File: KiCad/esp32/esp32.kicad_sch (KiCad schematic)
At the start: 2 parts, among them U1 ESD7104MUTAG, U2 ESP32-S3-MINI-1-N8

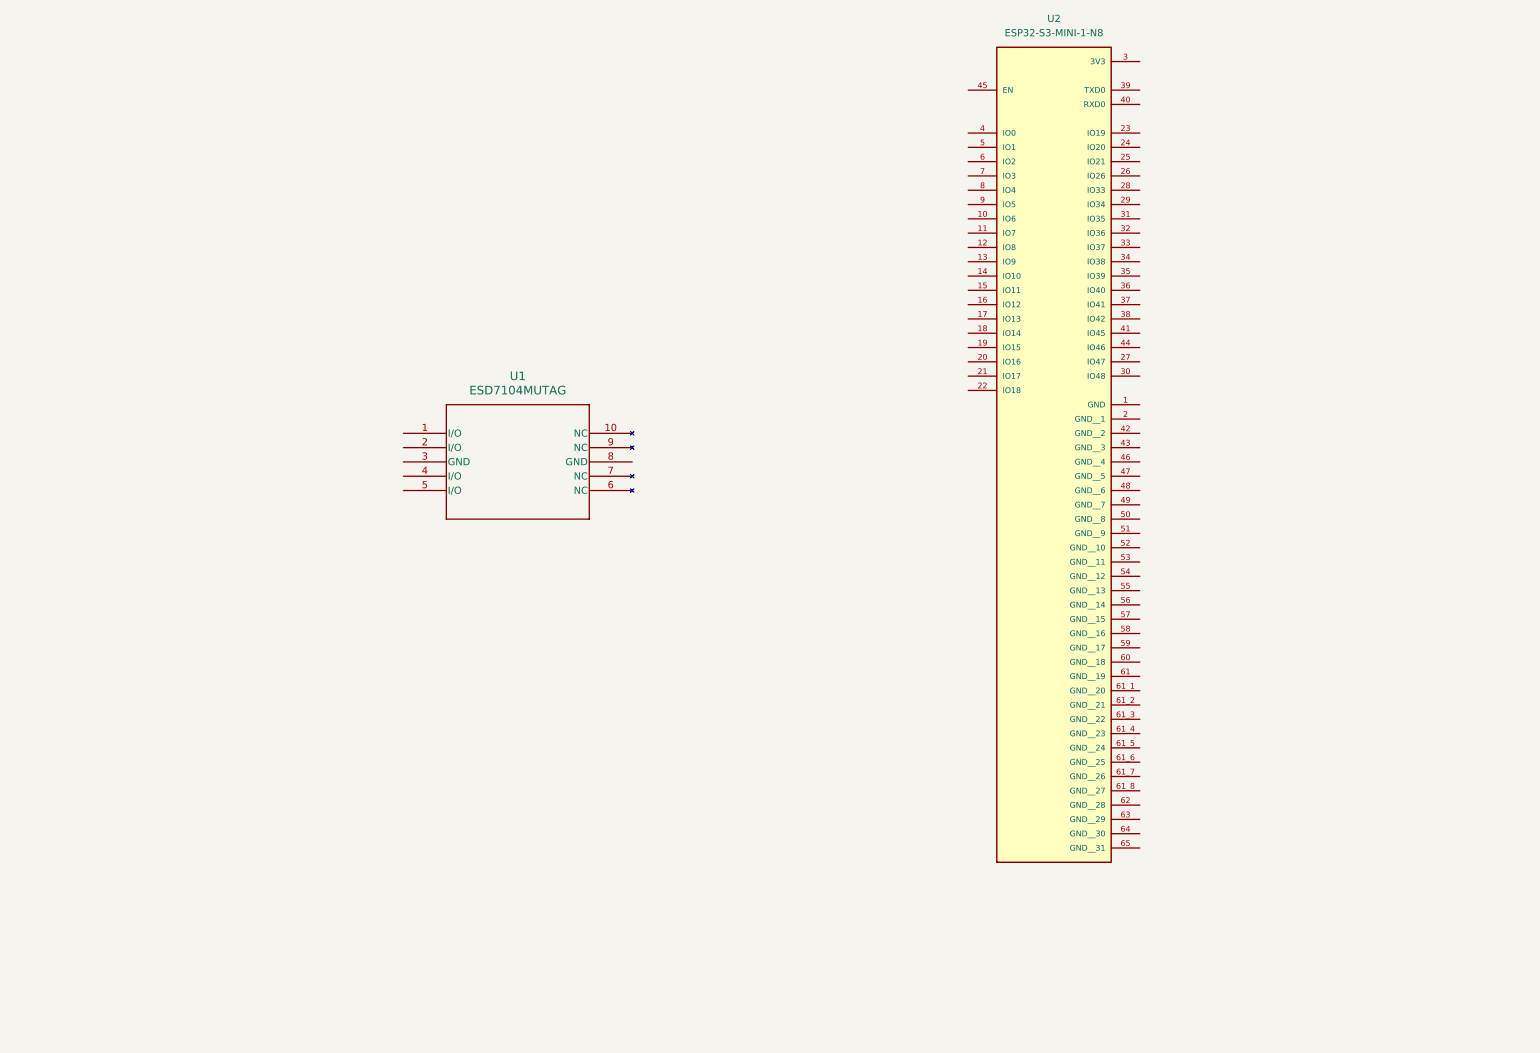
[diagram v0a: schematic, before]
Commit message: restructed the path and file strcter
upaded schiemate and update pcb layout
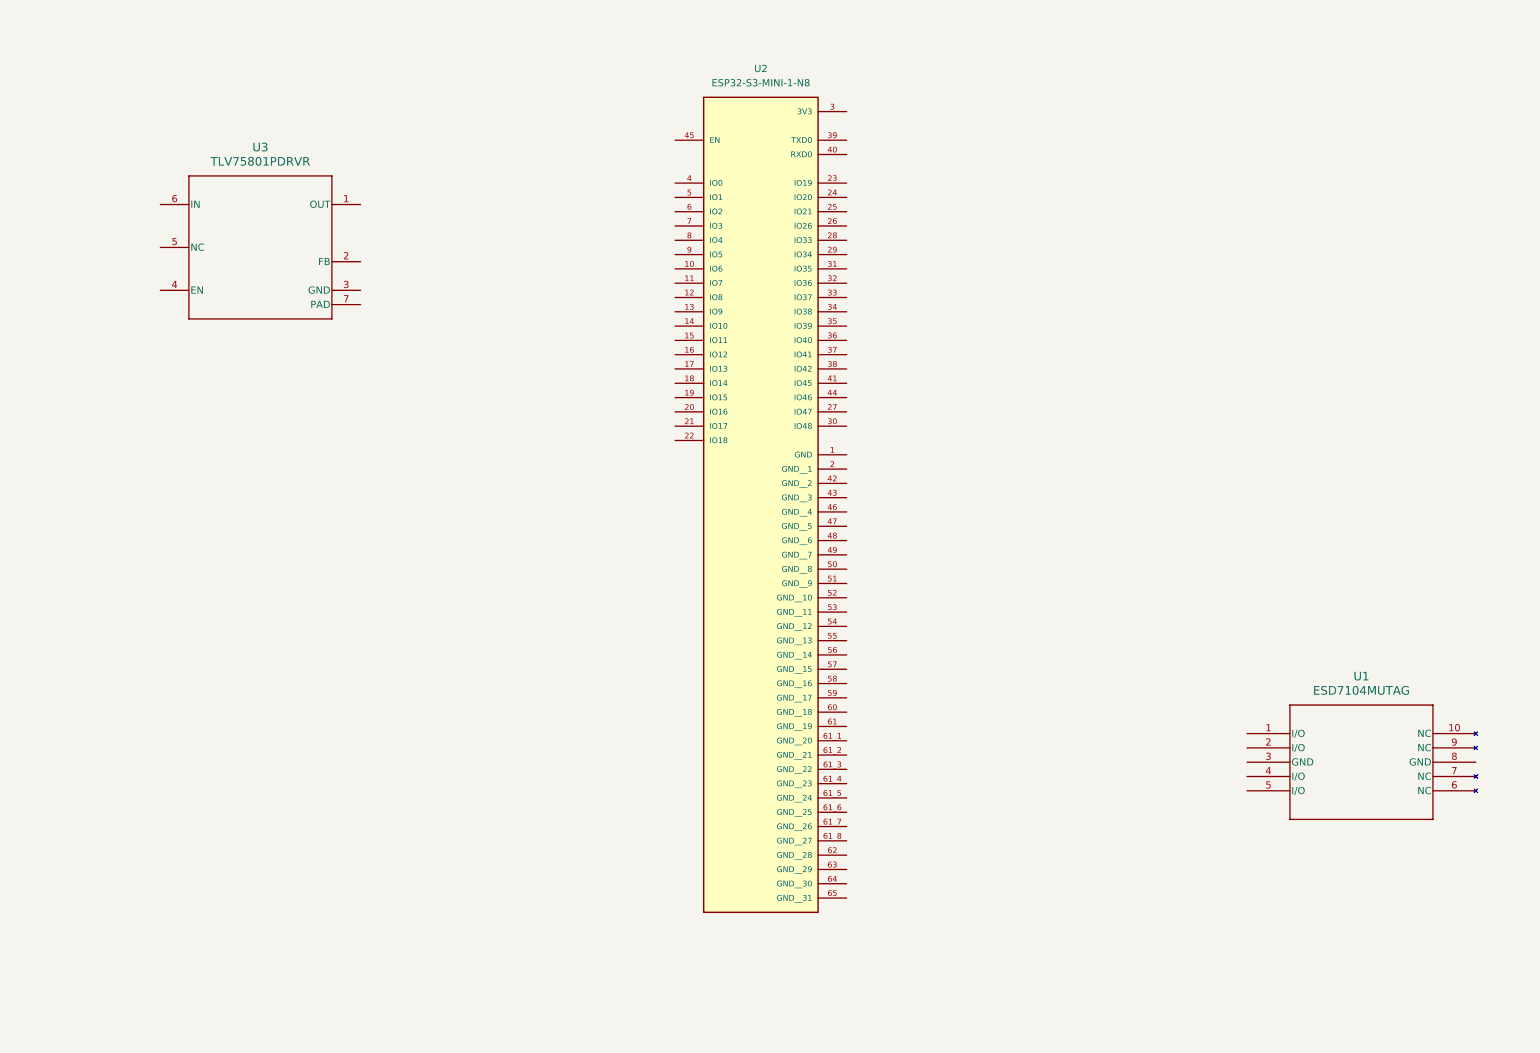
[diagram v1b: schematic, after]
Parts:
- removed U1: ESD7104MUTAG, footprints:UDFN10_ONS-L, symbol 2025-12-02_02-43-39:ESD7104MUTAG
- added U1: ESD7104MUTAG, Footprint:UDFN10_ONS, symbol ESD7104MUTAG:ESD7104MUTAG
- added U3: TLV75801PDRVR, Footprint:DRV0006A, symbol TLV75801PDRVR:TLV75801PDRVR
- U2: footprint ESP32_S3_MINI_1_N8:XCVR_ESP32-S3-MINI-1-N8 -> Footprint:XCVR_ESP32-S3-MINI-1-N8

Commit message: Added all symbols
dowloaded and added all symbols expect for boot/restart
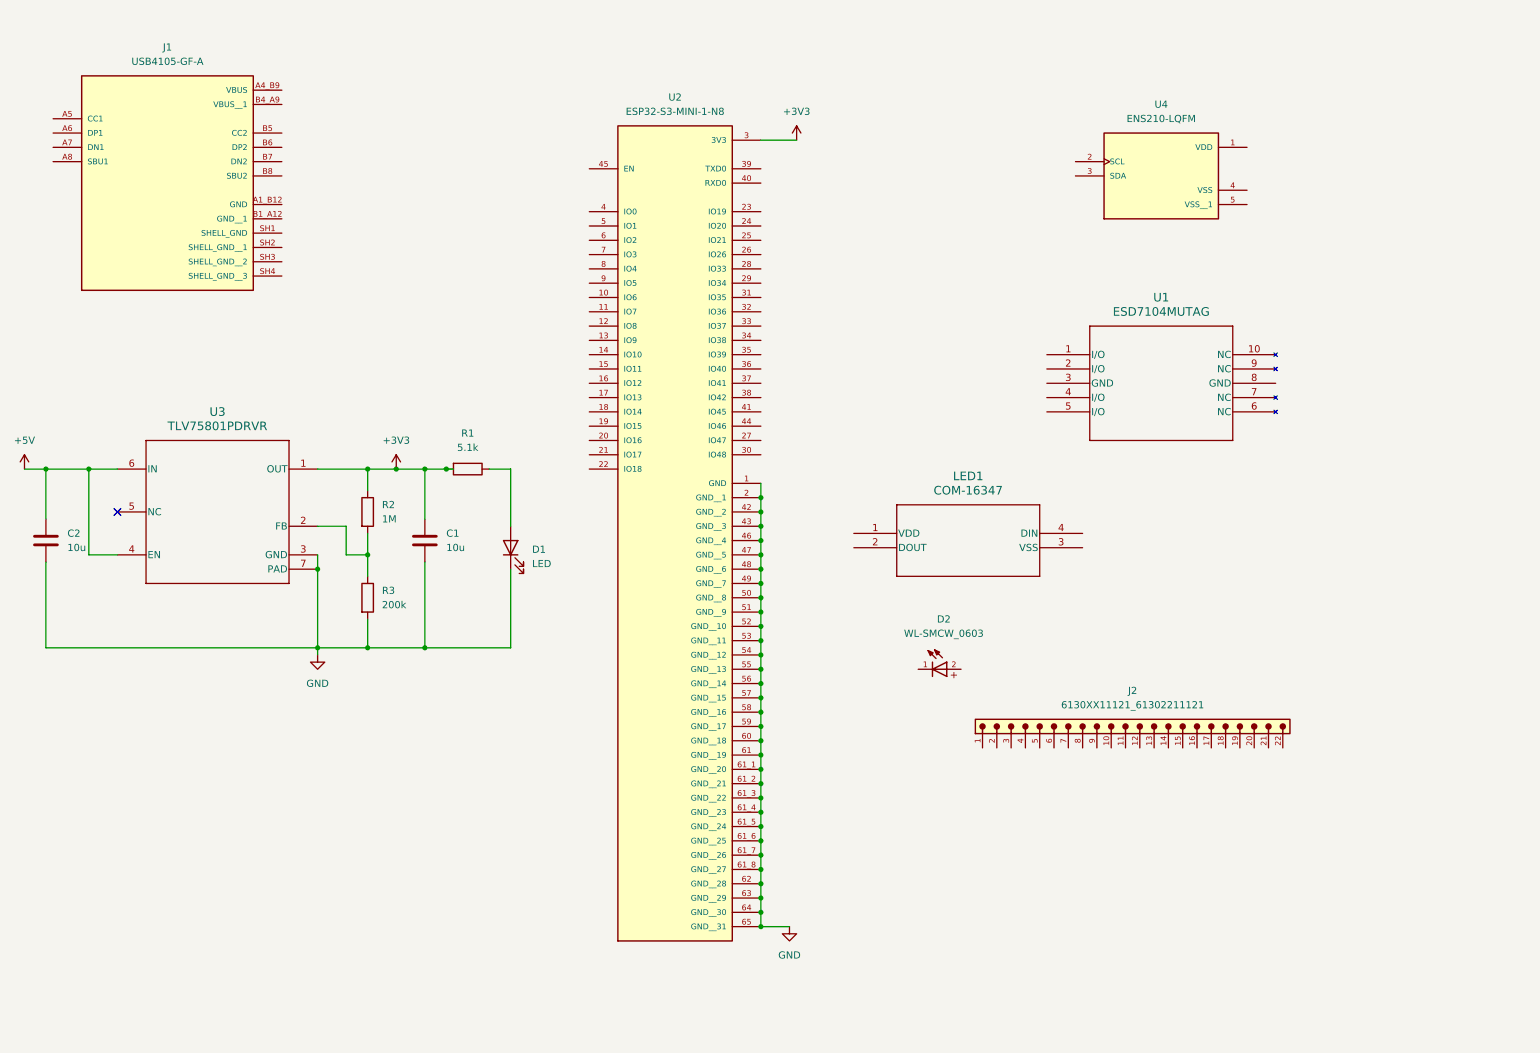
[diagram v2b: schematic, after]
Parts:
- added C1, C2: 10u, Capacitor_SMD:C_0603_1608Metric, symbol Device:C
- added D1: LED, LED_SMD:LED_0603_1608Metric, symbol Device:LED
- added D2: WL-SMCW_0603, WL-SMCW_0603:WL-SMCW_0603, symbol WL-SMCW_0603:WL-SMCW_0603
- added J1: USB4105-GF-A, USB4105-GF-A:GCT_USB4105-GF-A, symbol USB4105-GF-A:USB4105-GF-A
- added J2: 6130XX11121_61302211121, 6130XX11121_61302211121:61302211121, symbol 6130XX11121_61302211121:6130XX11121_61302211121
- added LED1: COM-16347, Footprint:COM-16347_SPK, symbol COM-16347:COM-16347
- added R1: 5.1k, Resistor_SMD:R_0603_1608Metric, symbol Device:R
- added R2: 1M, Resistor_SMD:R_0603_1608Metric, symbol Device:R
- added R3: 200k, Resistor_SMD:R_0603_1608Metric, symbol Device:R
- added U4: ENS210-LQFM, ENS210-LQFM:XDCR_ENS210-LQFM, symbol ENS210-LQFM:ENS210-LQFM
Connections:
- net +3V3: now reaches U3.1 (OUT)
- net +3V3: now also U2.3 (3V3), C1.1, R1.2, R2.1
- net at U3.2 (FB): now also R2.2, R3.1
- net GND: now reaches U3.3 (GND)
- net GND: now also U2.1 (GND), U2.2 (GND__1), U2.42 (GND__2), U2.43 (GND__3), U2.46 (GND__4), U2.47 (GND__5), U2.48 (GND__6), U2.49 (GND__7), U2.50 (GND__8), U2.51 (GND__9), U2.52 (GND__10), U2.53 (GND__11), U2.54 (GND__12), U2.55 (GND__13), U2.56 (GND__14), U2.57 (GND__15), U2.58 (GND__16), U2.59 (GND__17), U2.60 (GND__18), U2.61 (GND__19), U2.61_1 (GND__20), U2.61_2 (GND__21), U2.61_3 (GND__22), U2.61_4 (GND__23), U2.61_5 (GND__24), U2.61_6 (GND__25), U2.61_7 (GND__26), U2.61_8 (GND__27), U2.62 (GND__28), U2.63 (GND__29), U2.64 (GND__30), U2.65 (GND__31), U3.7 (PAD), C1.2, C2.2, D1.1 (K), R3.2
- net +5V: now reaches U3.4 (EN)
- net +5V: now also U3.6 (IN), C2.1
- new net: D1.2 (A), R1.1
- no-connect marks 0 -> 1
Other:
- company: (none) -> Yen-Vi Le
- title: (none) -> Custom ESP32 S3
- moved on the sheet: U1, U2, U3

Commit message: worked on schematic
Completed U4, led1, u3 usbj1, u5, j1, j3
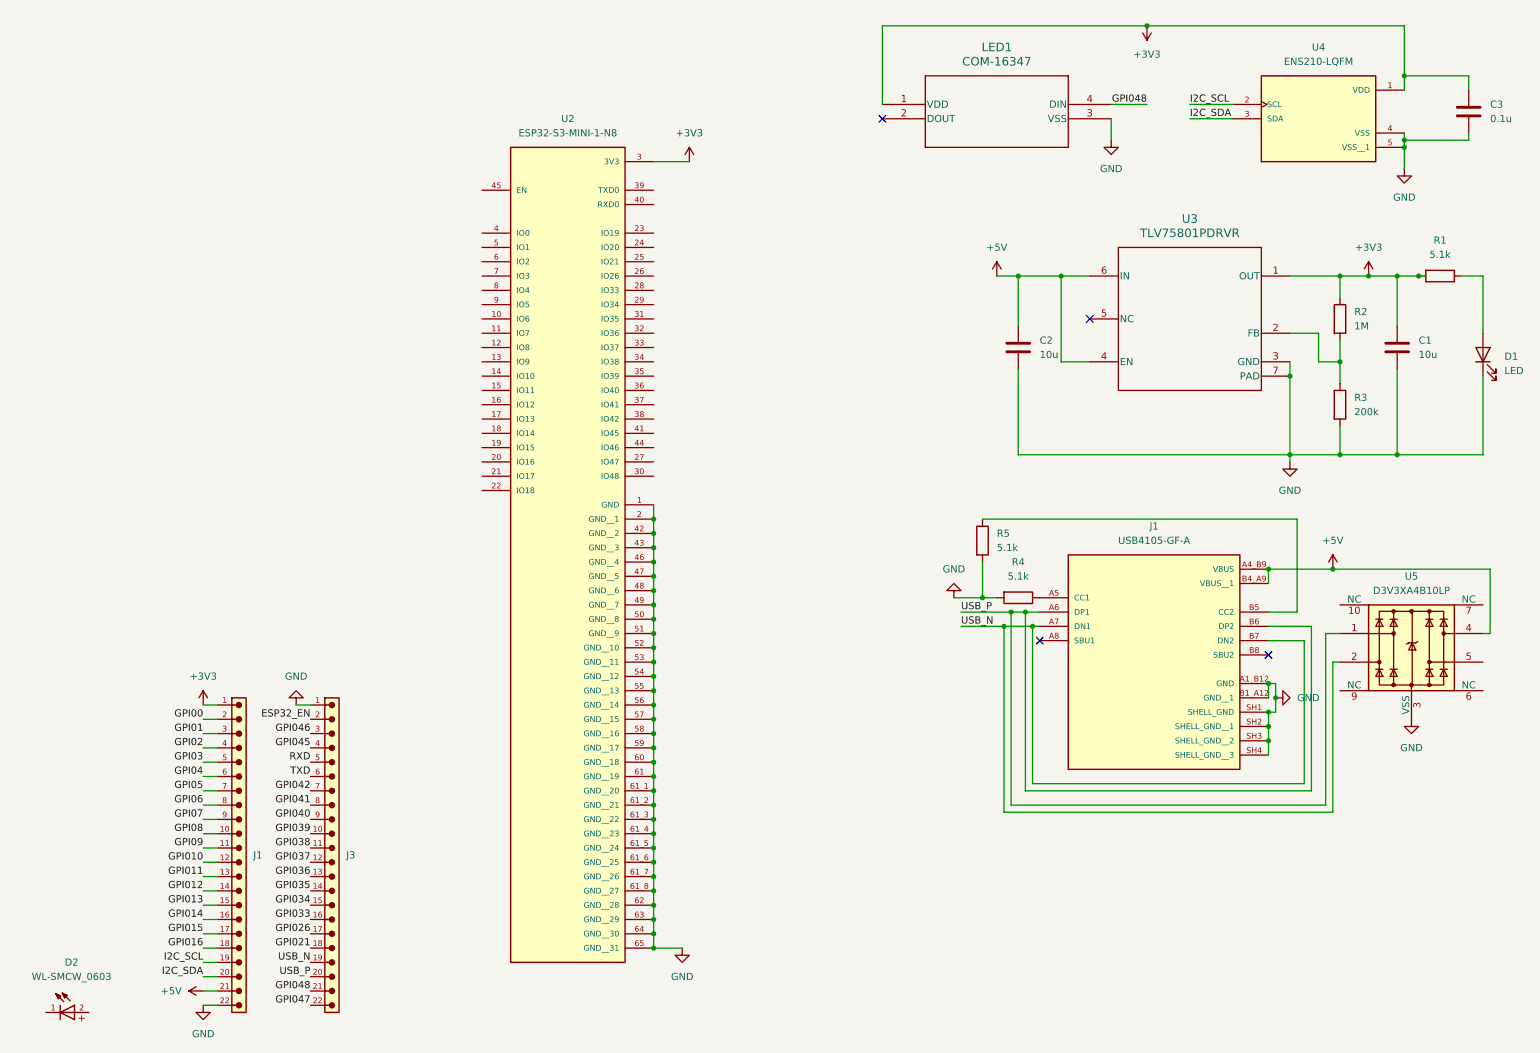
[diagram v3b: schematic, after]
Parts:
- removed U1: ESD7104MUTAG, Footprint:UDFN10_ONS, symbol ESD7104MUTAG:ESD7104MUTAG
- added C3: 0.1u, symbol Device:C
- added J3: 6130XX11121_61302211121, 6130XX11121_61302211121:61302211121, symbol 6130XX11121_61302211121:6130XX11121_61302211121
- added R4, R5: 5.1k, symbol Device:R
- added U5: D3V3XA4B10LP, Package_DFN_QFN:Diodes_UDFN-10_1.0x2.5mm_P0.5mm, symbol Power_Protection:D3V3XA4B10LP
- renumbered J2 to J1
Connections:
- net +3V3: now also J1.1, LED1.1 (VDD), U4.1 (VDD), C3.1
- net +5V: now also J1.21, J1.A4_B9 (VBUS), J1.B4_A9 (VBUS__1), U5.4
- net GND: now also J1.22, J1.A1_B12 (GND), J1.B1_A12 (GND__1), J1.SH1 (SHELL_GND), J1.SH2 (SHELL_GND__1), J1.SH3 (SHELL_GND__2), J1.SH4 (SHELL_GND__3), LED1.3 (VSS), U4.4 (VSS), U4.5 (VSS__1), C3.2, J3.1, R4.2, R5.2, U5.3 (VSS), U5.8 (VSS)
- net I2C_SCL: now reaches U4.2 (SCL)
- net I2C_SCL: now also J1.19
- net I2C_SDA: now reaches U4.3 (SDA)
- net I2C_SDA: now also J1.20
- net GPI08: now reaches J1.10
- net GPI09: now reaches J1.11
- net GPI010: now reaches J1.12
- net GPI011: now reaches J1.13
- net GPI012: now reaches J1.14
- net GPI013: now reaches J1.15
- net GPI014: now reaches J1.16
- net GPI015: now reaches J1.17
- net GPI016: now reaches J1.18
- net GPI00: now reaches J1.2
- net GPI01: now reaches J1.3
- net GPI02: now reaches J1.4
- net GPI03: now reaches J1.5
- net GPI04: now reaches J1.6
- net GPI05: now reaches J1.7
- net GPI06: now reaches J1.8
- net GPI07: now reaches J1.9
- net at J1.A5 (CC1): now also R4.1
- net USB_P: now reaches J1.A6 (DP1)
- net USB_P: now also J1.B6 (DP2), J3.20, U5.1
- net USB_N: now reaches J1.A7 (DN1)
- net USB_N: now also J1.B7 (DN2), J3.19, U5.2
- net at J1.B5 (CC2): now also R5.1
- net GPI048: now reaches LED1.4 (DIN)
- net GPI048: now also J3.21
- new net ESP32_EN: J3.2
- new net GPI021: J3.18
- new net GPI026: J3.17
- new net GPI033: J3.16
- new net GPI034: J3.15
- new net GPI035: J3.14
- new net GPI036: J3.13
- new net GPI037: J3.12
- new net GPI038: J3.11
- new net GPI039: J3.10
- new net GPI040: J3.9
- new net GPI041: J3.8
- new net GPI042: J3.7
- new net GPI045: J3.4
- new net GPI046: J3.3
- new net GPI047: J3.22
- new net RXD: J3.5
- new net TXD: J3.6
- no-connect marks 1 -> 4
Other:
- moved on the sheet: C1, C2, D1, D2, J1, LED1, R1, R2, R3, U2, U3, U4

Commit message: added reset and boot
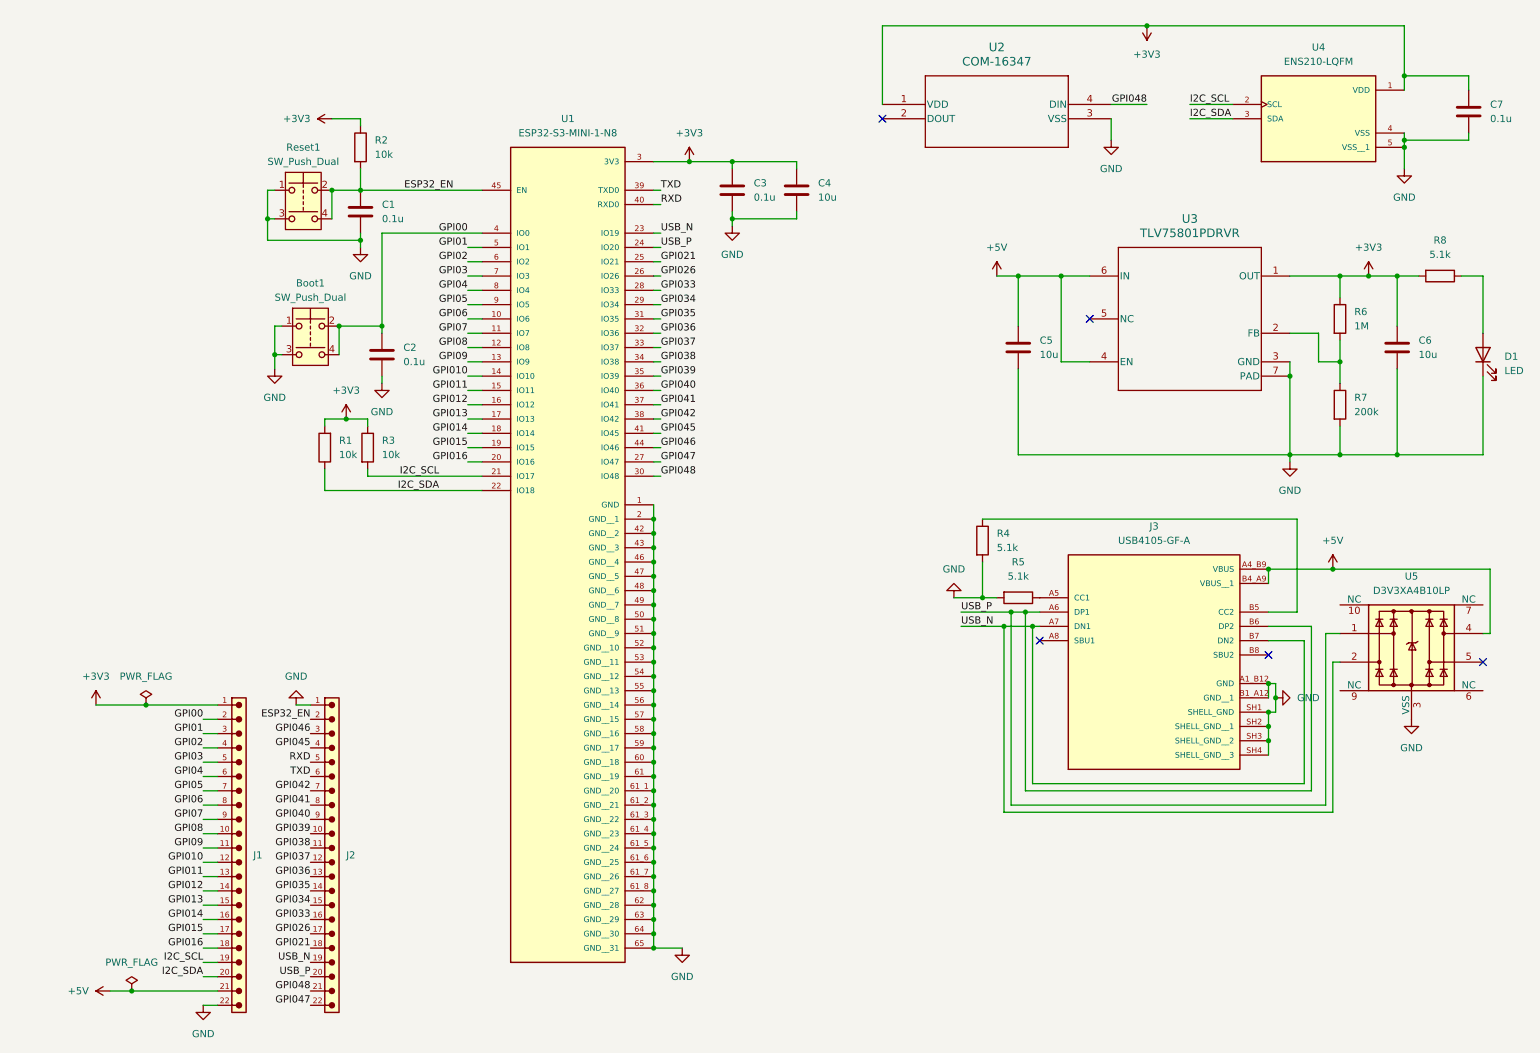
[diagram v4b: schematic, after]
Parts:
- removed D2: WL-SMCW_0603, WL-SMCW_0603:WL-SMCW_0603, symbol WL-SMCW_0603:WL-SMCW_0603
- added Boot1, Reset1: SW_Push_Dual, symbol Switch:SW_Push_Dual
- added C1, C2, C3: 0.1u, symbol Device:C
- added C4: 10u, symbol Device:C
- added R1, R2, R3: 10k, symbol Device:R
- renumbered C2 to C5, C1 to C6, C3 to C7, J3 to J2, J1 to J3, R5 to R4, R4 to R5, R2 to R6, R3 to R7, R1 to R8, U2 to U1, LED1 to U2
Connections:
- net +3V3: now also C3.1, C4.1, R1.2, R2.1, R3.1
- net ESP32_EN: now also U1.45 (EN), C1.1, R2.2, Reset1.2, Reset1.4
- net GND: now also Boot1.1, Boot1.3, C1.2, C2.2, C3.2, C4.2, Reset1.1, Reset1.3
- net GPI00: now also U1.4 (IO0), Boot1.2, Boot1.4, C2.1
- net GPI01: now also U1.5 (IO1)
- net GPI010: now also U1.14 (IO10)
- net GPI011: now also U1.15 (IO11)
- net GPI012: now also U1.16 (IO12)
- net GPI013: now also U1.17 (IO13)
- net GPI014: now also U1.18 (IO14)
- net GPI015: now also U1.19 (IO15)
- net GPI016: now also U1.20 (IO16)
- net GPI02: now also U1.6 (IO2)
- net GPI021: now also U1.25 (IO21)
- net GPI026: now also U1.26 (IO26)
- net GPI03: now also U1.7 (IO3)
- net GPI033: now also U1.28 (IO33)
- net GPI034: now also U1.29 (IO34)
- net GPI035: now also U1.31 (IO35)
- net GPI036: now also U1.32 (IO36)
- net GPI037: now also U1.33 (IO37)
- net GPI038: now also U1.34 (IO38)
- net GPI039: now also U1.35 (IO39)
- net GPI04: now also U1.8 (IO4)
- net GPI040: now also U1.36 (IO40)
- net GPI041: now also U1.37 (IO41)
- net GPI042: now also U1.38 (IO42)
- net GPI045: now also U1.41 (IO45)
- net GPI046: now also U1.44 (IO46)
- net GPI047: now also U1.27 (IO47)
- net GPI048: now also U1.30 (IO48)
- net GPI05: now also U1.9 (IO5)
- net GPI06: now also U1.10 (IO6)
- net GPI07: now also U1.11 (IO7)
- net GPI08: now also U1.12 (IO8)
- net GPI09: now also U1.13 (IO9)
- net I2C_SCL: now also U1.21 (IO17), R3.2
- net I2C_SDA: now also U1.22 (IO18), R1.1
- net RXD: now also U1.40 (RXD0)
- net TXD: now also U1.39 (TXD0)
- net USB_N: now also U1.23 (IO19)
- net USB_P: now also U1.24 (IO20)
- no-connect marks 4 -> 5
